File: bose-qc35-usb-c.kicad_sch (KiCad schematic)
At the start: 37 parts, among them J1 502426-2030, J2 TYPE-C-31-M-12, J3 51281-0594, Q1 BC846BM3T5G, U1 TPS25200

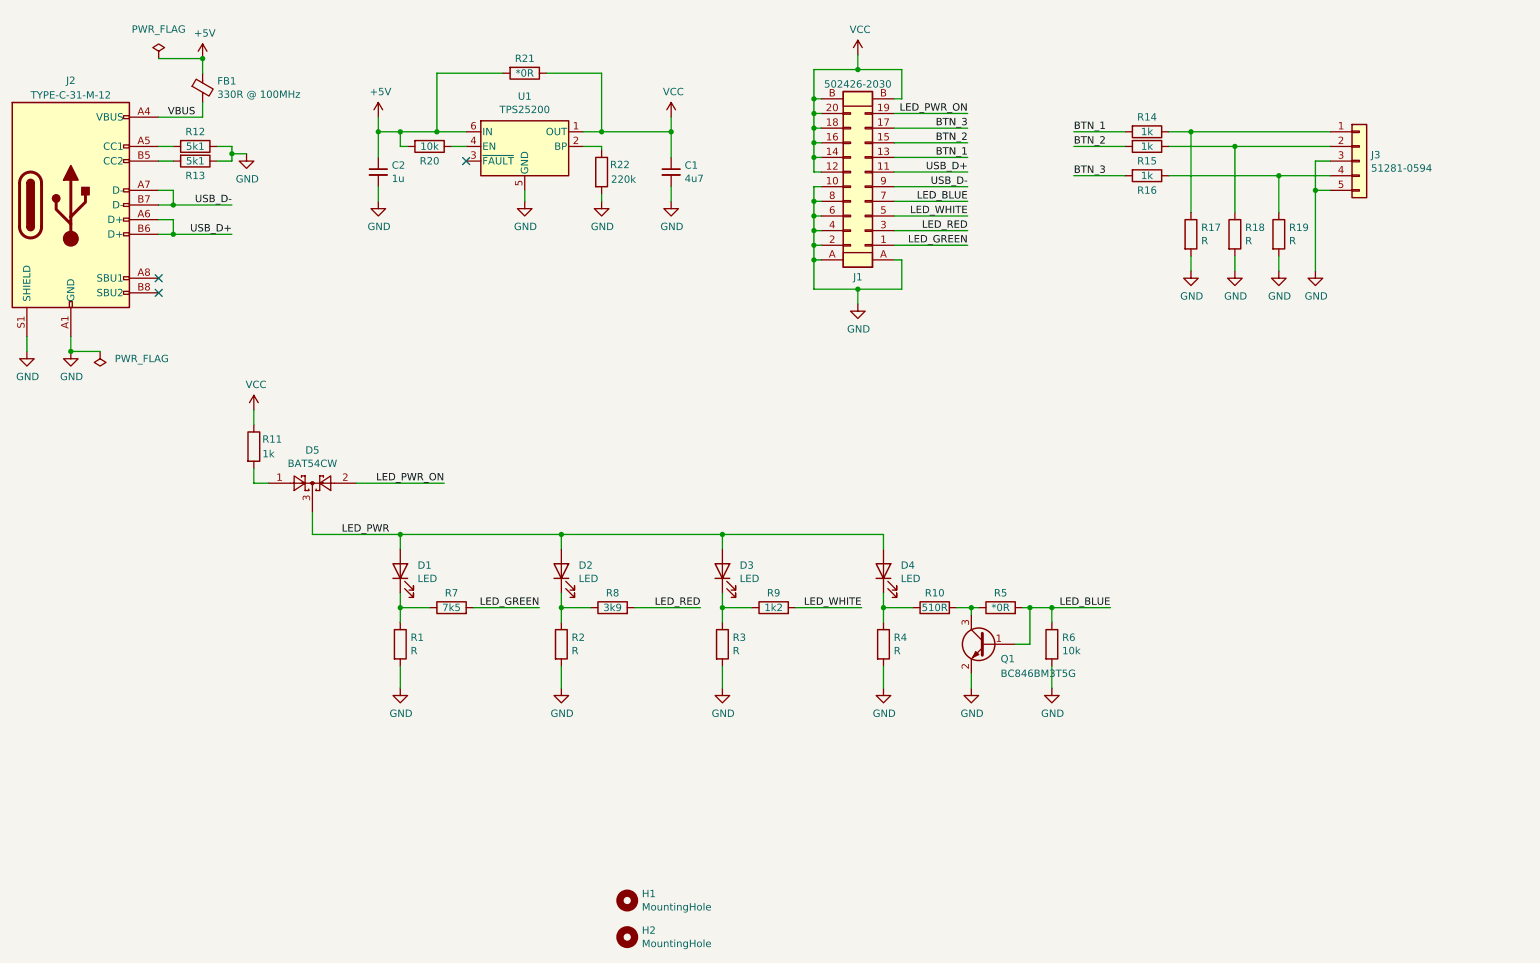
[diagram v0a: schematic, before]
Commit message: Clarify component choices
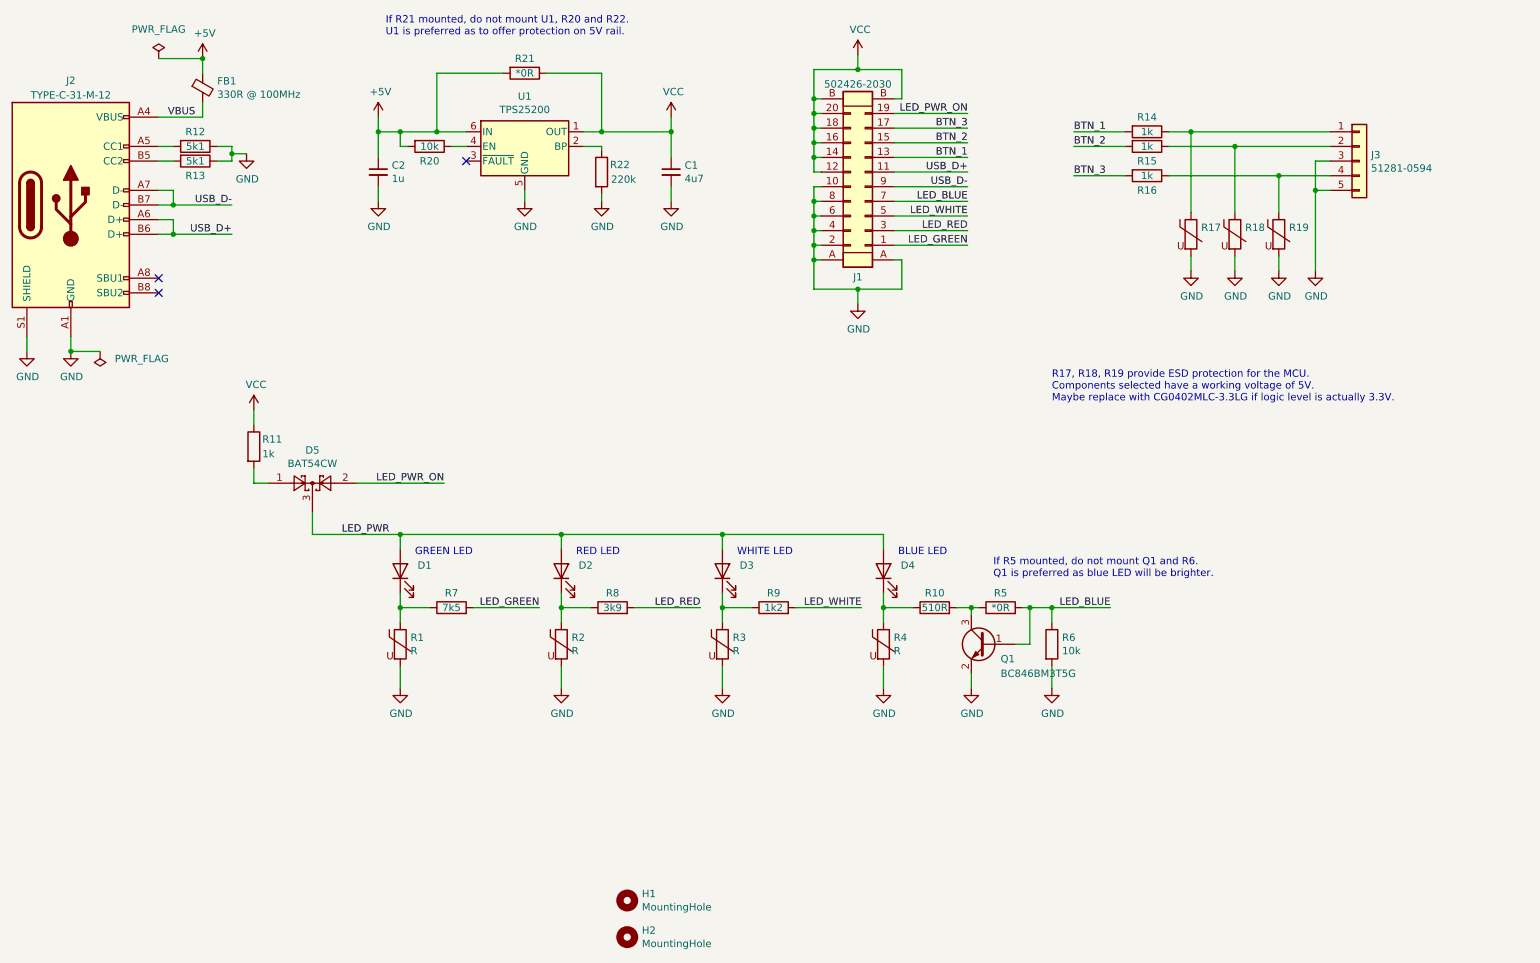
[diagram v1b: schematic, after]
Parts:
- D1, D3, D4: value LED -> (none); footprint LED_SMD:LED_0603_1608Metric -> (none)
- D2: value LED -> (none)
- R1, R2, R3, R4: symbol Device:R -> Device:Varistor
- R17, R18, R19: value R -> (none); footprint Resistor_SMD:R_0402_1005Metric -> (none); symbol Device:R -> Device:Varistor
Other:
- note added: "BLUE LED"
- note added: "GREEN LED"
- note added: "If R21 mounted, do not mount U1, R20 and R22. U1 is preferred as to offer protection on 5V rail."
- note added: "If R5 mounted, do not mount Q1 and R6. Q1 is preferred as blue LED will be brighter."
- note added: "R17, R18, R19 provide ESD protection for the MCU. Components selected have a working voltage of 5V. Maybe replace with CG0402MLC-3.3LG if logic level is actually 3.3V."
- note added: "RED LED"
- note added: "WHITE LED"

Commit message: Update more component values
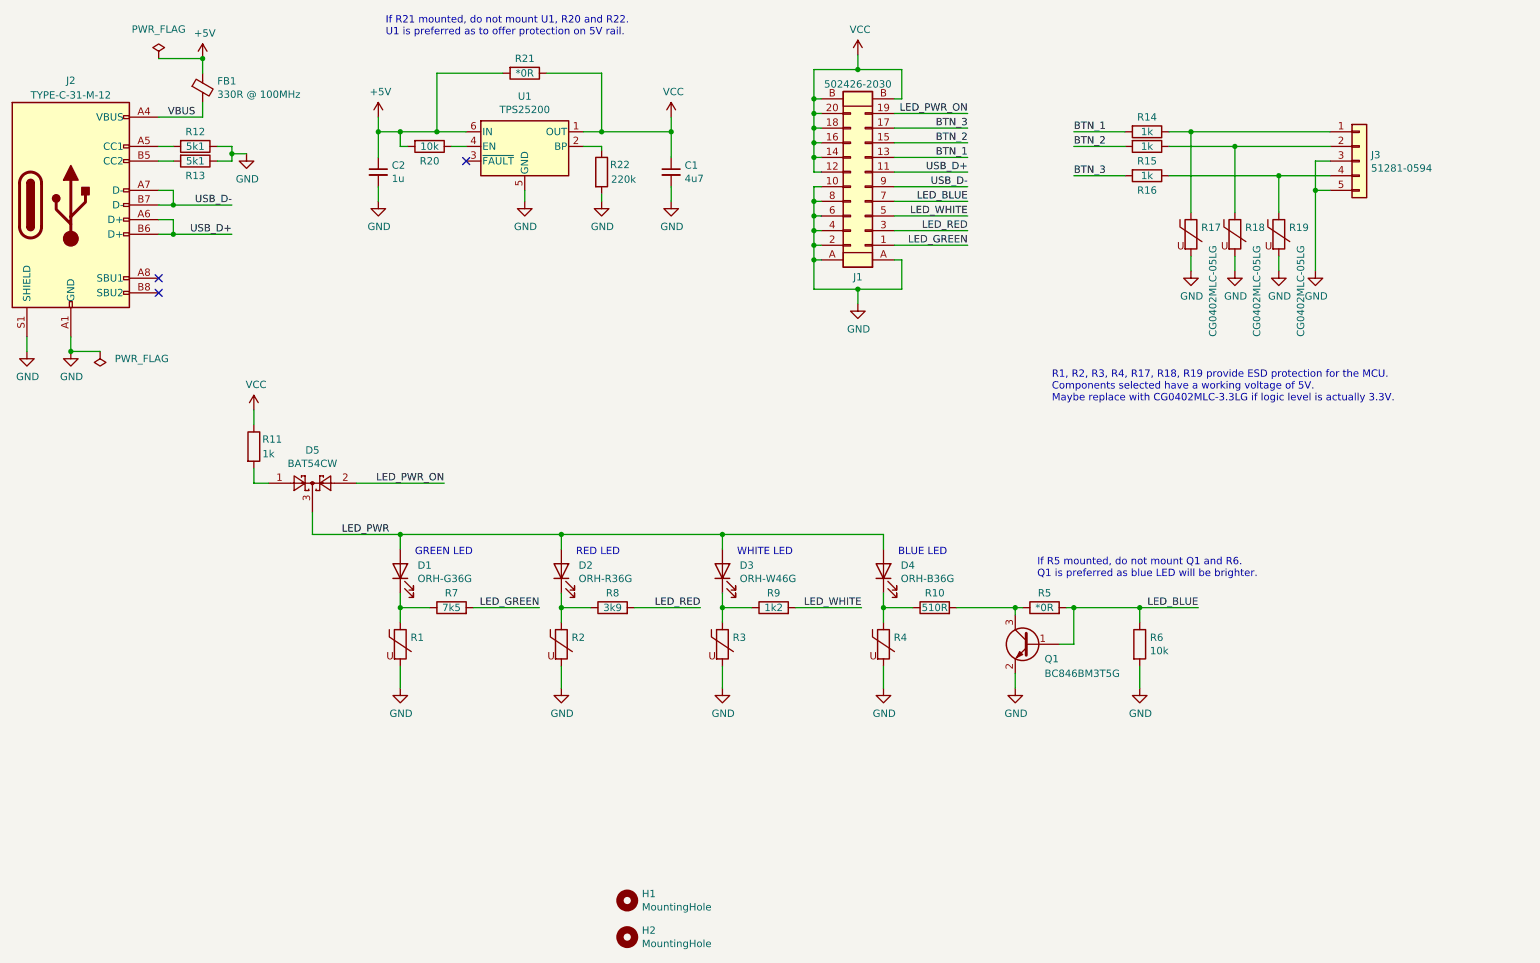
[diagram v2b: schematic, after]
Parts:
- D1: value (none) -> ORH-G36G; footprint (none) -> LED_SMD:LED_0603_1608Metric
- D2: value (none) -> ORH-R36G
- D3: value (none) -> ORH-W46G; footprint (none) -> LED_SMD:LED_0603_1608Metric
- D4: value (none) -> ORH-B36G; footprint (none) -> LED_SMD:LED_0603_1608Metric
- R1, R2, R3, R4: value R -> (none); footprint Resistor_SMD:R_0402_1005Metric -> (none)
- R17, R18, R19: value (none) -> CG0402MLC-05LG; footprint (none) -> Resistor_SMD:R_0402_1005Metric
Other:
- note added: "R1, R2, R3, R4, R17, R18, R19 provide ESD protection for the MCU. Components selected have a working voltage of 5V. Maybe replace with CG0402MLC-3.3LG if logic level is actually 3.3V."
- note removed: "R17, R18, R19 provide ESD protection for the MCU. Components selected have a working voltage of 5V. Maybe replace with CG0402MLC-3.3LG if logic level is actually 3.3V."
- moved on the sheet: Q1, R5, R6

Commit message: Update shematic for calrity and to kicad 7
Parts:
- R1, R2, R3, R4: value (none) -> CG0402MLC-05LG; footprint (none) -> Resistor_SMD:R_0402_1005Metric; now not fitted
- R17, R18, R19: now not fitted
- R21, R5: value *0R -> 0R; now not fitted

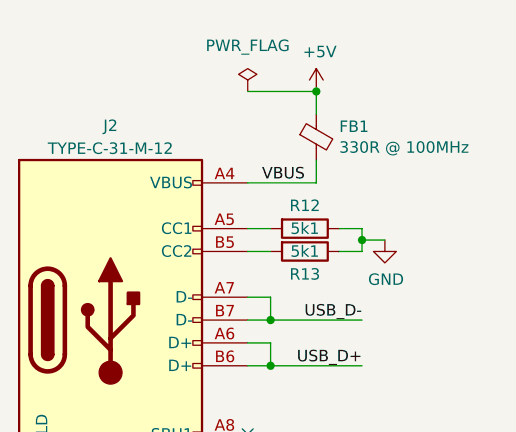
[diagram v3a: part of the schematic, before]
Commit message: Use alternative USB C port which doesn't require modification
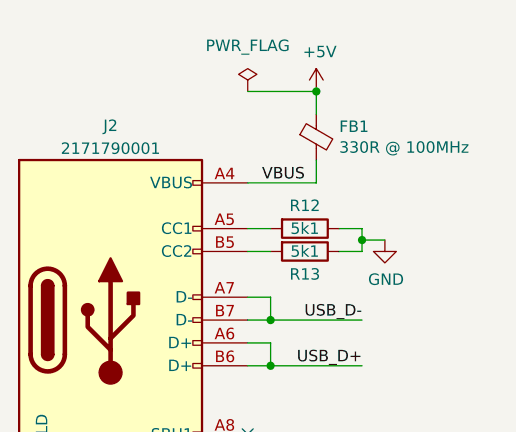
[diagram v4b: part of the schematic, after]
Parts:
- J2: value TYPE-C-31-M-12 -> 2171790001; footprint Connector_USB:USB_C_Receptacle_HRO_TYPE-C-31-M-12 -> library:USB_C_Receptacle_Molex_2171790001
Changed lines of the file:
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@@
       (effects (font (size 1.27 1.27)))
     )
-    (property "Value" "TYPE-C-31-M-12" (at 41.91 35.56 0)
+    (property "Value" "2171790001" (at 41.91 35.56 0)
       (effects (font (size 1.27 1.27)))
     )
-    (property "Footprint" "Connector_USB:USB_C_Receptacle_HRO_TYPE-C-31-M-12" (at 45.72 54.61 0)
+    (property "Footprint" "library:USB_C_Receptacle_Molex_2171790001" (at 45.72 54.61 0)
       (effects (font (size 1.27 1.27)) hide)
     )
-    (property "Datasheet" "https://datasheet.lcsc.com/szlcsc/1811131825_Korean-Hroparts-Elec-TYPE-C-31-M-12_C165948.pdf" (at 45.72 54.61 0)
+    (property "Datasheet" "https://www.molex.com/en-us/products/part-detail/2171790001?display=pdf" (at 45.72 54.61 0)
       (effects (font (size 1.27 1.27)) hide)
     )

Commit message: Add LCSC part numbers
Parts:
- C1: LCSC (none) -> C23733
- C2: LCSC (none) -> C52923
- D1: LCSC (none) -> C7371905
- D2: LCSC (none) -> C2286
- D3: LCSC (none) -> C2290
- D4: LCSC (none) -> C193191
- D5: LCSC (none) -> C22392482
- FB1: LCSC (none) -> C160975
- J1: LCSC (none) -> C563934
- J2: LCSC (none) -> C29780877
- J3: LCSC (none) -> C127344
- Q1: LCSC (none) -> C232536
- R1, R17, R18, R19, R2, R3, R4: LCSC (none) -> C711709
- R10: LCSC (none) -> C25123
- R11, R14, R15, R16: LCSC (none) -> C11702
- R12, R13: LCSC (none) -> C25905
- R20, R6: LCSC (none) -> C25744
- R22: LCSC (none) -> C25767
- R7: LCSC (none) -> C137934
- R8: LCSC (none) -> C131467
- R9: LCSC (none) -> C25862
- U1: LCSC (none) -> C128401
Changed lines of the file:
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@@
+      (effects (font (size 1.27 1.27)) hide)
+    )
+    (property "LCSC" "C563934" (at 179.705 51.435 0)
       (effects (font (size 1.27 1.27)) hide)
     )
@@
       (effects (font (size 1.27 1.27)) hide)
     )
+    (property "LCSC" "C7371905" (at 102.0572 117.1194 0)
+      (effects (font (size 1.27 1.27)) hide)
+    )
     (pin "1")
     (pin "2")
@@
       (effects (font (size 1.27 1.27)) hide)
     )
+    (property "LCSC" "C2286" (at 129.9972 117.1194 0)
+      (effects (font (size 1.27 1.27)) hide)
+    )
     (pin "1")
     (pin "2")
@@
       (effects (font (size 1.27 1.27)) hide)
     )
+    (property "LCSC" "C2290" (at 157.9372 117.1194 0)
+      (effects (font (size 1.27 1.27)) hide)
+    )
     (pin "1")
     (pin "2")
@@
     )
     (property "Datasheet" "~" (at 182.88 118.11 0)
+      (effects (font (size 1.27 1.27)) hide)
+    )
+    (property "LCSC" "C193191" (at 185.8772 117.1194 0)
       (effects (font (size 1.27 1.27)) hide)
     )
@@
       (effects (font (size 1.27 1.27)) hide)
     )
+    (property "LCSC" "C711709" (at 99.06 130.81 0)
+      (effects (font (size 1.27 1.27)) hide)
+    )
     (pin "1")
     (pin "2")
@@
       (effects (font (size 1.27 1.27)) hide)
     )
+    (property "LCSC" "C711709" (at 127 130.81 0)
+      (effects (font (size 1.27 1.27)) hide)
+    )
     (pin "1")
     (pin "2")
@@
       (effects (font (size 1.27 1.27)) hide)
     )
+    (property "LCSC" "C711709" (at 154.94 130.81 0)
+      (effects (font (size 1.27 1.27)) hide)
+    )
     (pin "1")
     (pin "2")
@@
       (effects (font (size 1.27 1.27)) hide)
     )
+    (property "LCSC" "C711709" (at 182.88 130.81 0)
+      (effects (font (size 1.27 1.27)) hide)
+    )
     (pin "1")
     (pin "2")
@@
     )
     (property "Datasheet" "http://www.st.com/content/ccc/resource/technical/document/datasheet/29/10/f7/87/2f/66/47/f4/DM00076097.pdf/files/DM00076097.pdf/jcr:content/translations/en.DM00076097.pdf" (at 120.65 44.45 0)
+      (effects (font (size 1.27 1.27)) hide)
+    )
+    (property "LCSC" "C128401" (at 120.65 35.7632 0)
       (effects (font (size 1.27 1.27)) hide)
     )
@@
       (effects (font (size 1.27 1.27)) hide)
     )
+    (property "LCSC" "C127344" (at 267.462 45.9232 0)
+      (effects (font (size 1.27 1.27)) hide)
+    )
     (pin "1")
     (pin "2")
@@
     )
     (property "Datasheet" "https://www.molex.com/en-us/products/part-detail/2171790001?display=pdf" (at 45.72 54.61 0)
+      (effects (font (size 1.27 1.27)) hide)
+    )
+    (property "LCSC" "C29780877" (at 41.91 33.02 0)
       (effects (font (size 1.27 1.27)) hide)
     )
@@
       (effects (font (size 1.27 1.27)) hide)
     )
+    (property "LCSC" "C52923" (at 97.5868 47.7266 0)
+      (effects (font (size 1.27 1.27)) hide)
+    )
     (pin "1")
     (pin "2")
@@
     )
     (property "Datasheet" "~" (at 208.28 130.81 0)
+      (effects (font (size 1.27 1.27)) hide)
+    )
+    (property "LCSC" "C232536" (at 210.82 133.35 0)
       (effects (font (size 1.27 1.27)) hide)
     )
@@
       (effects (font (size 1.27 1.27)) hide)
     )
+    (property "LCSC" "C25744" (at 104.14 44.45 0)
+      (effects (font (size 1.27 1.27)) hide)
+    )
     (pin "1")
     (pin "2")
@@
     )
     (property "Datasheet" "~" (at 227.33 130.81 0)
+      (effects (font (size 1.27 1.27)) hide)
+    )
+    (property "LCSC" "C25744" (at 227.33 130.81 0)
       (effects (font (size 1.27 1.27)) hide)
     )
@@
       (effects (font (size 1.27 1.27)) hide)
     )
+    (property "LCSC" "C22392482" (at 83.82 97.155 0)
+      (effects (font (size 1.27 1.27)) hide)
+    )
     (pin "1")
     (pin "2")
@@
     )
     (property "Datasheet" "~" (at 107.95 124.46 0)
+      (effects (font (size 1.27 1.27)) hide)
+    )
+    (property "LCSC" "C137934" (at 107.95 121.92 0)
       (effects (font (size 1.27 1.27)) hide)
     )
@@
       (effects (font (size 1.27 1.27)) hide)
     )
+    (property "LCSC" "C131467" (at 135.89 121.92 0)
+      (effects (font (size 1.27 1.27)) hide)
+    )
     (pin "1")
     (pin "2")
@@
       (effects (font (size 1.27 1.27)) hide)
     )
+    (property "LCSC" "C25862" (at 163.83 121.92 0)
+      (effects (font (size 1.27 1.27)) hide)
+    )
     (pin "1")
     (pin "2")
@@
       (effects (font (size 1.27 1.27)) hide)
     )
+    (property "LCSC" "C25123" (at 191.77 121.92 0)
+      (effects (font (size 1.27 1.27)) hide)
+    )
     (pin "1")
     (pin "2")
@@
       (effects (font (size 1.27 1.27)) hide)
     )
+    (property "LCSC" "C11702" (at 76.835 95.25 0)
+      (effects (font (size 1.27 1.27)) hide)
+    )
     (pin "1")
     (pin "2")
@@
       (effects (font (size 1.27 1.27)) hide)
     )
+    (property "LCSC" "C23733" (at 148.3868 47.7266 0)
+      (effects (font (size 1.27 1.27)) hide)
+    )
     (pin "1")
     (pin "2")
@@
       (effects (font (size 1.27 1.27)) hide)
     )
+    (property "LCSC" "C25767" (at 137.16 47.625 0)
+      (effects (font (size 1.27 1.27)) hide)
+    )
     (pin "1")
     (pin "2")
@@
       (effects (font (size 1.27 1.27)) hide)
     )
+    (property "LCSC" "C160975" (at 67.31 33.1216 0)
+      (effects (font (size 1.27 1.27)) hide)
+    )
     (pin "1")
     (pin "2")
@@
       (effects (font (size 1.27 1.27)) hide)
     )
+    (property "LCSC" "C25905" (at 63.5 41.91 0)
+      (effects (font (size 1.27 1.27)) hide)
+    )
     (pin "1")
     (pin "2")
@@
       (effects (font (size 1.27 1.27)) hide)
     )
+    (property "LCSC" "C25905" (at 63.5 49.53 0)
+      (effects (font (size 1.27 1.27)) hide)
+    )
     (pin "1")
     (pin "2")
@@
       (effects (font (size 1.27 1.27)) hide)
     )
+    (property "LCSC" "C11702" (at 228.6 41.91 0)
+      (effects (font (size 1.27 1.27)) hide)
+    )
     (pin "1")
     (pin "2")
@@
       (effects (font (size 1.27 1.27)) hide)
     )
+    (property "LCSC" "C11702" (at 228.6 44.45 0)
+      (effects (font (size 1.27 1.27)) hide)
+    )
     (pin "1")
     (pin "2")
@@
     )
     (property "Datasheet" "~" (at 228.6 49.53 0)
+      (effects (font (size 1.27 1.27)) hide)
+    )
+    (property "LCSC" "C11702" (at 228.6 52.07 0)
       (effects (font (size 1.27 1.27)) hide)
     )
@@
       (effects (font (size 1.27 1.27)) hide)
     )
+    (property "LCSC" "C711709" (at 236.22 59.69 0)
+      (effects (font (size 1.27 1.27)) hide)
+    )
     (pin "1")
     (pin "2")
@@
       (effects (font (size 1.27 1.27)) hide)
     )
+    (property "LCSC" "C711709" (at 243.84 59.69 0)
+      (effects (font (size 1.27 1.27)) hide)
+    )
     (pin "1")
     (pin "2")
@@
       (effects (font (size 1.27 1.27)) hide)
     )
+    (property "LCSC" "C711709" (at 251.46 59.69 0)
+      (effects (font (size 1.27 1.27)) hide)
+    )
